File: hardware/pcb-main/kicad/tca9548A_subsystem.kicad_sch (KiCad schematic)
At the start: 6 parts, among them U4 TCA9548APWR

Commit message: Finished sensor redesign
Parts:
- U4: footprint TCA9548:SOP65P640X120-24N -> motion-play-footprints:SOP65P640X120-24N; symbol TCA9548:TCA9548APWR -> motion-play-symbols:TCA9548APWR; Description_1 8-channel 1.65- to 5.5-V I2C/SMBus switch with reset & voltage translation -> 8-channel 1.65- to 5.5-V I2C/SMBus switch with reset & voltage translation; DigiKey_Part_Number (none) -> 296-34905-1-ND
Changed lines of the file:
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@@
 	)
 	(symbol
-		(lib_id "TCA9548:TCA9548APWR")
+		(lib_id "motion-play-symbols:TCA9548APWR")
 		(at 163.83 91.44 0)
 		(unit 1)
@@
 			)
 		)
-		(property "Footprint" "TCA9548:SOP65P640X120-24N"
+		(property "Footprint" "motion-play-footprints:SOP65P640X120-24N"
 			(at 163.83 91.44 0)
 			(effects
@@
 			)
 		)
-		(property "Description_1" "\n                        \n                            8-channel 1.65- to 5.5-V I2C/SMBus switch with reset & voltage translation\n                        \n"
+		(property "Description_1" "8-channel 1.65- to 5.5-V I2C/SMBus switch with reset & voltage translation"
 			(at 163.83 91.44 0)
 			(effects
@@
 				(hide yes)
 			)
+		)
+		(property "DigiKey_Part_Number" "296-34905-1-ND"
+			(at 163.83 91.44 0)
+			(effects
+				(font
+					(size 1.27 1.27)
+				)
+				(justify bottom)
+				(hide yes)
+			)

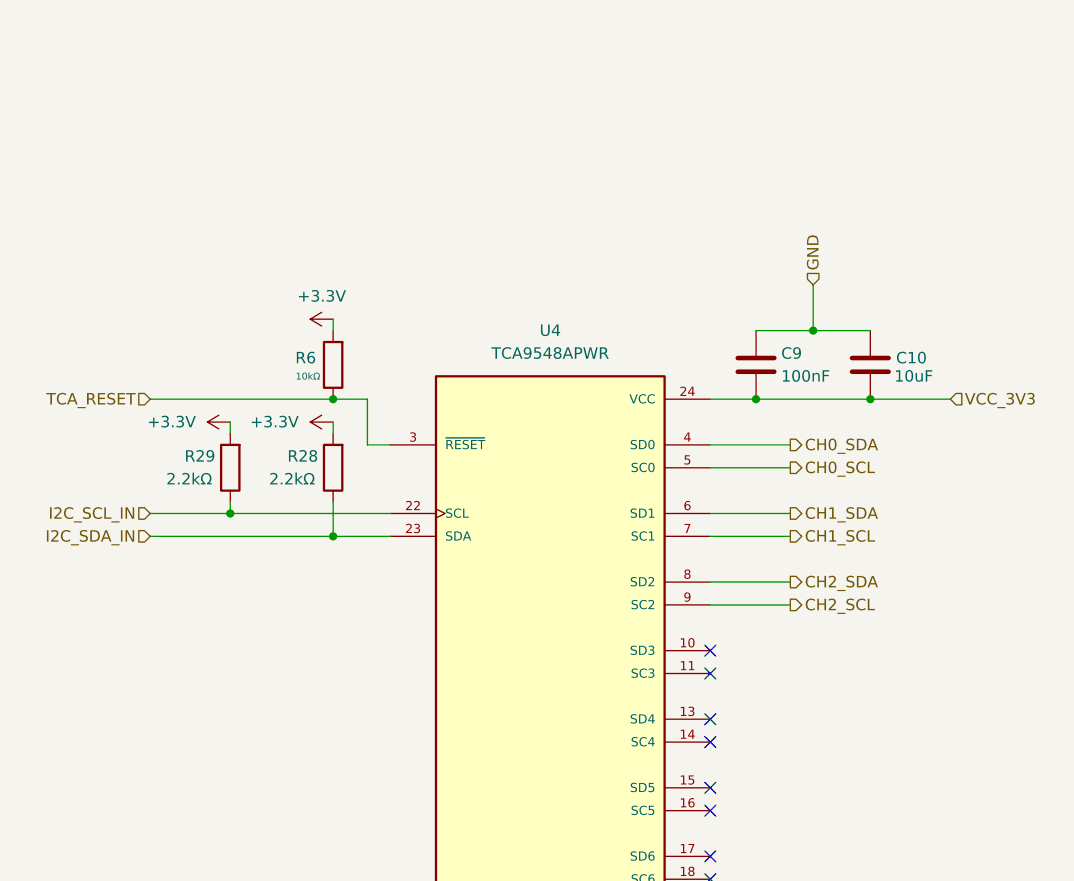
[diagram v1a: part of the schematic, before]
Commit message: Complete Phase 3a: annotate power, MCU, I2C mux, and sensor connector blocks
Annotated 31/37 components across 4 functional blocks (power, mcu, i2c_mux,
sensor_connectors) with ai_function, ai_block, ai_role, and ai_critical_specs
properties. Remaining 6 components are LED controller block (Phase 3b).
Added 10 verification test questions for Phase 3c. KiCad round-trip confirmed
all ai_ properties survive native save.

Made-with: Cursor
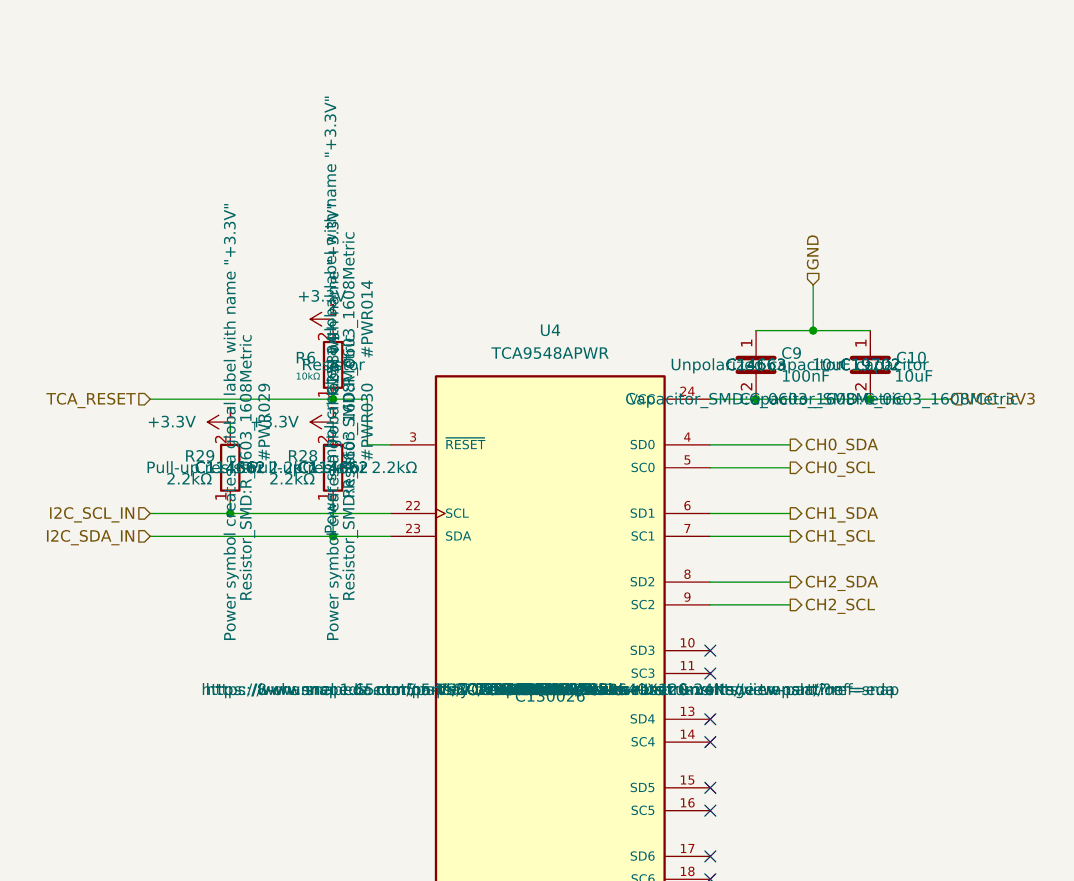
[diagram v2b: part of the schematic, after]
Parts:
- C10: ai_block (none) -> i2c_mux; ai_critical_specs (none) -> 10uF, 0603; ai_function (none) -> Bulk decoupling capacitor for TCA9548A; ai_role (none) -> decoupling
- C9: ai_block (none) -> i2c_mux; ai_critical_specs (none) -> 100nF, 0603, placed close to VCC pin; ai_function (none) -> High-frequency decoupling capacitor for TCA9548A; ai_role (none) -> decoupling
- R28: ai_block (none) -> i2c_mux; ai_critical_specs (none) -> 2.2k to +3.3V, sized for 400kHz operation; ai_function (none) -> I2C SDA pull-up on upstream bus between MCU and TCA9548A; ai_role (none) -> pull_up
- R29: ai_block (none) -> i2c_mux; ai_critical_specs (none) -> 2.2k to +3.3V, sized for 400kHz operation; ai_function (none) -> I2C SCL pull-up on upstream bus between MCU and TCA9548A; ai_role (none) -> pull_up
- R6: ai_block (none) -> i2c_mux; ai_critical_specs (none) -> 10k to +3.3V; ai_function (none) -> Active-low reset pull-up for TCA9548A, keeps mux out of res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; ai_role (none) -> pull_up
- U4: ai_block (none) -> i2c_mux; ai_critical_specs (none) -> Address 0x70 (A0=A1=A2=GND), 3 channels used of 8, 400kHz c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; ai_function (none) -> TCA9548A 8-channel I2C multiplexer, routes MCU I2C bus to 3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; ai_role (none) -> multiplexer

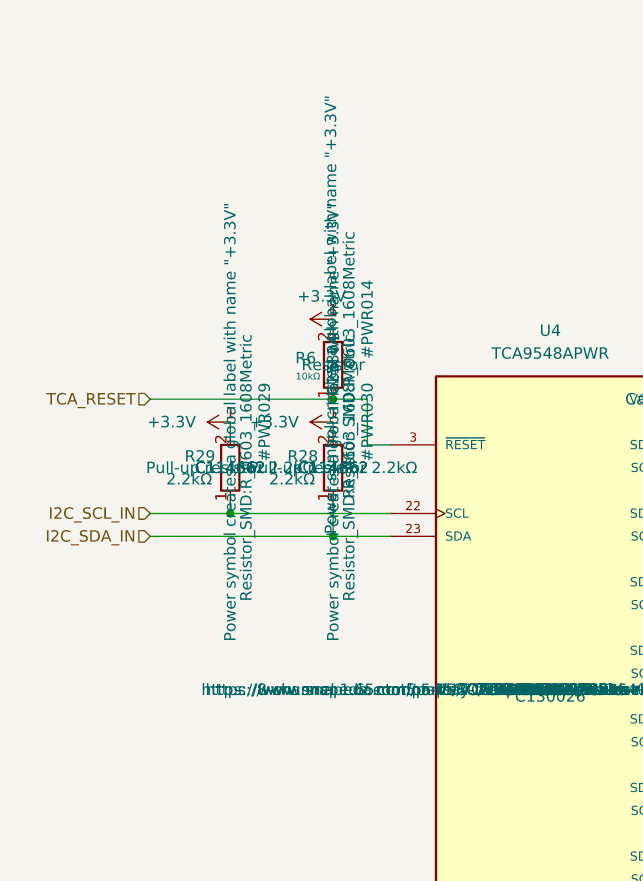
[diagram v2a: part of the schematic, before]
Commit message: Complete Phase 3b: annotate LED controller block, nets, and functional blocks
- Annotated final 6 components (IC1 level shifter, F1 fuse, R27 sense
  resistor, C7/C8 caps, J3 LED connector) → 37/37 components (100%)
- Added net annotations for all 26 nets (type, protocol, direction, description)
- Defined 5 functional blocks: power, mcu, i2c_mux, sensor_connectors,
  led_controller — with descriptions, component membership, and design notes
- Added top-level description and sheet_interface descriptions
- Re-extracted with --previous merge; KiCad round-trip save applied to all sheets

Made-with: Cursor
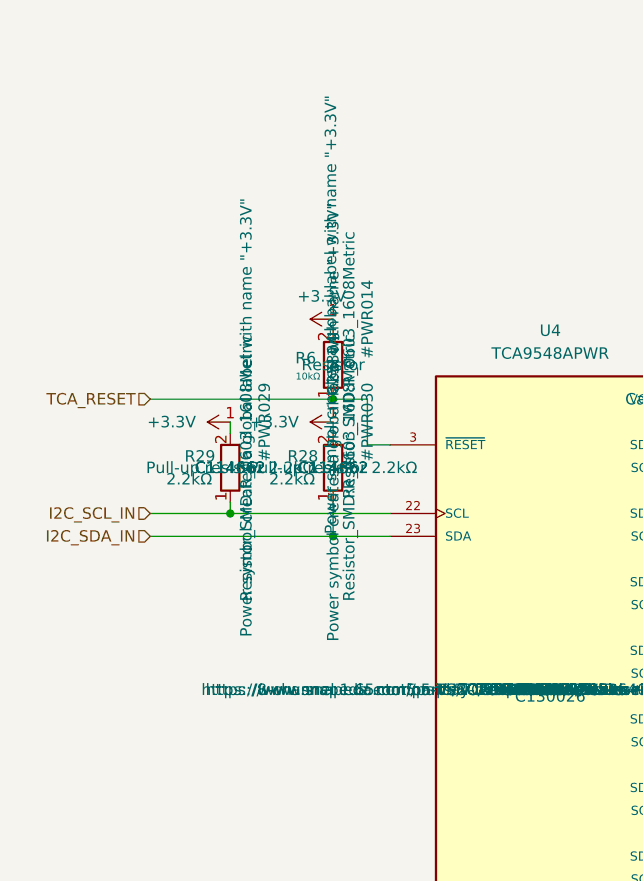
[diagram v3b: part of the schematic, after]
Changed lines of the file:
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@@
 		(on_board yes)
 		(dnp no)
-		(fields_autoplaced yes)
 		(property "Reference" "#PWR029"
 			(at 132.08 60.96 0)
@@
 		)
 		(property "Description" "Power symbol creates a global label with name \"+3.3V\""
-			(at 128.27 60.96 0)
+			(at 130.048 60.452 0)
 			(effects
 				(font

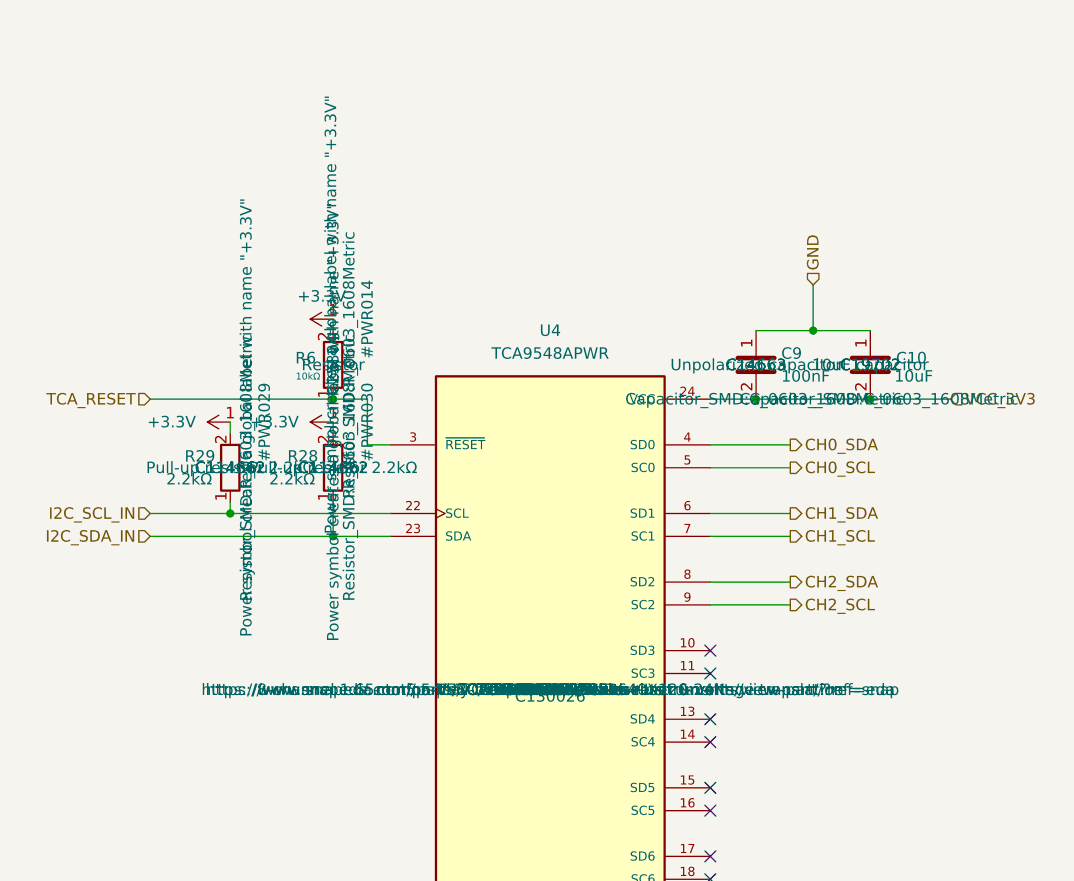
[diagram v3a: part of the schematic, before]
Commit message: Integrate power management sub-sheet into root schematic (Phase 3.6)
- Delete J2 (DWEII USB-C module) and D1 (Schottky) from root sheet
- Add hierarchical sheet reference to power_management.kicad_sch
- Wire 6 sheet pins: +5V, GND, +3.3V, I2C_SDA, I2C_SCL, CHRG_INT
- Connect CHRG_INT to GPIO 21 (U2 pin 19)
- Hide non-essential property labels (Description, Datasheet, etc.)
  across all original schematic sheets — only Reference and Value visible
- ERC: 0 errors on root/LED/TCA9548A sheets, 4 expected power_pin
  warnings on power management sheet (net labels vs PWR_FLAG)

Made-with: Cursor
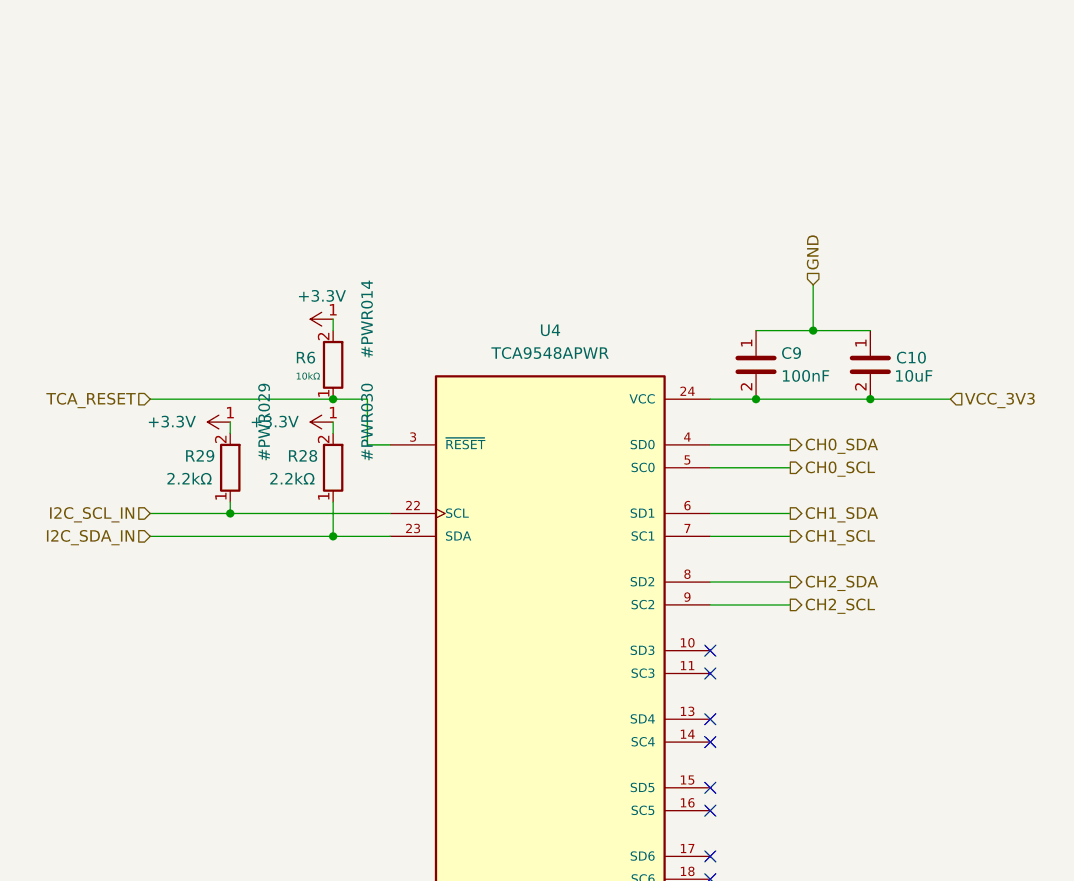
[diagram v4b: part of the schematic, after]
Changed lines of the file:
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@@
 					(size 1.27 1.27)
 				)
+				(hide yes)
 			)
 		)
@@
 					(size 1.27 1.27)
 				)
+				(hide yes)
 			)
 		)
@@
 					(size 1.27 1.27)
 				)
+				(hide yes)
 			)
 		)
@@
 					(size 1.27 1.27)
 				)
+				(hide yes)
 			)
 		)
@@
 					(size 1.27 1.27)
 				)
+				(hide yes)
 			)
 		)
@@
 					(size 1.27 1.27)
 				)
+				(hide yes)
 			)
 		)
@@
 					(size 1.27 1.27)
 				)
+				(hide yes)
 			)
 		)
@@
 					(size 1.27 1.27)
 				)
+				(hide yes)
 			)
 		)
@@
 					(size 1.27 1.27)
 				)
+				(hide yes)
 			)
 		)
@@
 					(size 1.27 1.27)
 				)
+				(hide yes)
 			)
 		)
@@
 					(size 1.27 1.27)
 				)
+				(hide yes)
 			)
 		)
@@
 					(size 1.27 1.27)
 				)
+				(hide yes)
 			)
 		)
@@
 					(size 1.27 1.27)
 				)
+				(hide yes)
 			)
 		)
@@
 					(size 1.27 1.27)
 				)
+				(hide yes)
 			)
 		)
@@
 					(size 1.27 1.27)
 				)
+				(hide yes)
 			)
 		)
@@
 					(size 1.27 1.27)
 				)
+				(hide yes)
 			)
 		)
@@
 					(size 1.27 1.27)
 				)
+				(hide yes)
 			)
 		)
@@
 					(size 1.27 1.27)
 				)
+				(hide yes)
 			)
 		)
@@
 					(size 1.27 1.27)
 				)
+				(hide yes)
 			)
 		)
@@
 					(size 1.27 1.27)
 				)
+				(hide yes)
 			)
 		)
@@
 					(size 1.27 1.27)
 				)
+				(hide yes)
 			)
 		)
@@
 					(size 1.27 1.27)
 				)
+				(hide yes)
 			)
 		)
@@
 					(size 1.27 1.27)
 				)
+				(hide yes)
 			)
 		)
@@
 					(size 1.27 1.27)
 				)
+				(hide yes)
 			)
 		)
@@
 					(size 1.27 1.27)
 				)
+				(hide yes)
 			)
 		)
@@
 					(size 1.27 1.27)
 				)
+				(hide yes)
 			)
 		)
@@
 					(size 1.27 1.27)
 				)
+				(hide yes)
 			)
 		)
@@
 					(size 1.27 1.27)
 				)
+				(hide yes)
 			)
 		)
@@
 				)
 				(justify bottom)
+				(hide yes)
 			)
 		)
@@
 					(size 1.27 1.27)
 				)
+				(hide yes)
 			)
 		)
@@
 					(size 1.27 1.27)
 				)
+				(hide yes)
 			)
 		)
@@
 				)
 				(justify bottom)
+				(hide yes)
 			)
 		)
@@
 				)
 				(justify bottom)
+				(hide yes)
 			)
 		)
@@
 				)
 				(justify bottom)
+				(hide yes)
 			)
 		)
@@
 				)
 				(justify bottom)
+				(hide yes)
 			)
 		)
@@
 				)
 				(justify bottom)
+				(hide yes)
 			)
 		)
@@
 				)
 				(justify bottom)
+				(hide yes)
 			)
 		)
@@
 				)
 				(justify bottom)
+				(hide yes)
 			)
 		)
@@
 				)
 				(justify bottom)
+				(hide yes)
 			)
 		)
@@
 				)
 				(justify bottom)
+				(hide yes)
 			)
 		)
@@
 				)
 				(justify bottom)
+				(hide yes)
 			)
 		)
@@
 				)
 				(justify bottom)
+				(hide yes)
 			)
 		)
@@
 				)
 				(justify bottom)
+				(hide yes)
 			)
 		)
@@
 					(size 1.27 1.27)
 				)
+				(hide yes)
 			)
 		)
@@
 				)
 				(justify bottom)
+				(hide yes)
 			)
 		)
@@
 					(size 1.27 1.27)
 				)
+				(hide yes)
 			)
 		)
@@
 					(size 1.27 1.27)
 				)
+				(hide yes)
 			)
 		)
@@
 					(size 1.27 1.27)
 				)
+				(hide yes)
 			)
 		)
@@
 					(size 1.27 1.27)
 				)
+				(hide yes)
 			)
 		)
@@
 					(size 1.27 1.27)
 				)
-			)
-		)
+				(hide yes)
+			)
+		)
